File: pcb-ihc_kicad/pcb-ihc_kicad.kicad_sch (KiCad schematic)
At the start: 76 parts, among them J2 Screw_Terminal_01x01, J3 Screw_Terminal_01x01, J4 Screw_Terminal_01x01, J5 Screw_Terminal_01x01, J6 Screw_Terminal_01x01, J7 Screw_Terminal_01x01, J8 Screw_Terminal_01x01, J9 Screw_Terminal_01x01, K1 RT314A24, K2 RT314A24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

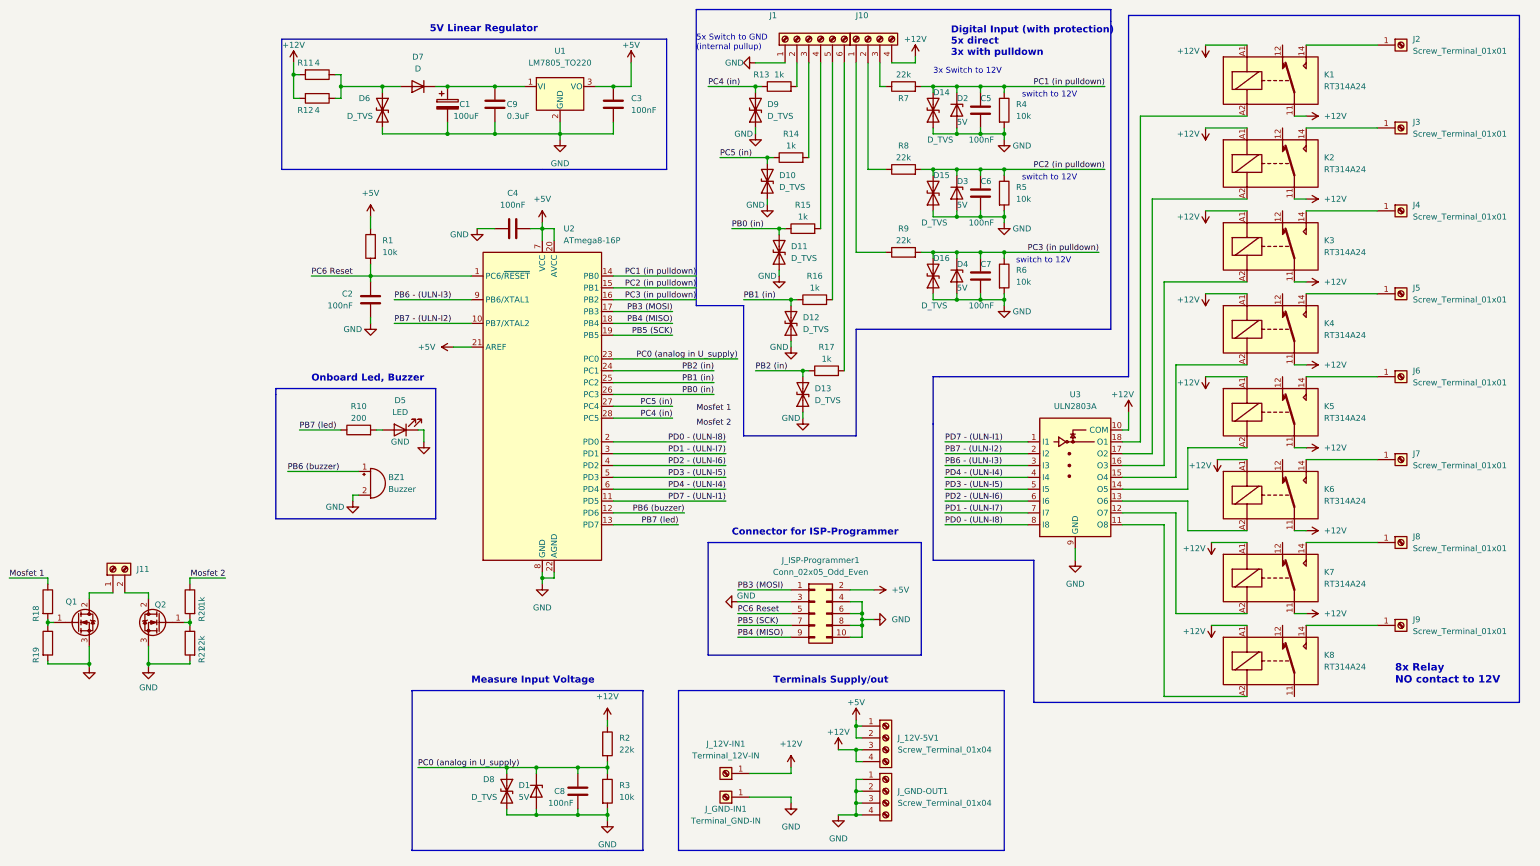
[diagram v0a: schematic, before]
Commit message: Add 2x Mosfet, Change labels, Change layout
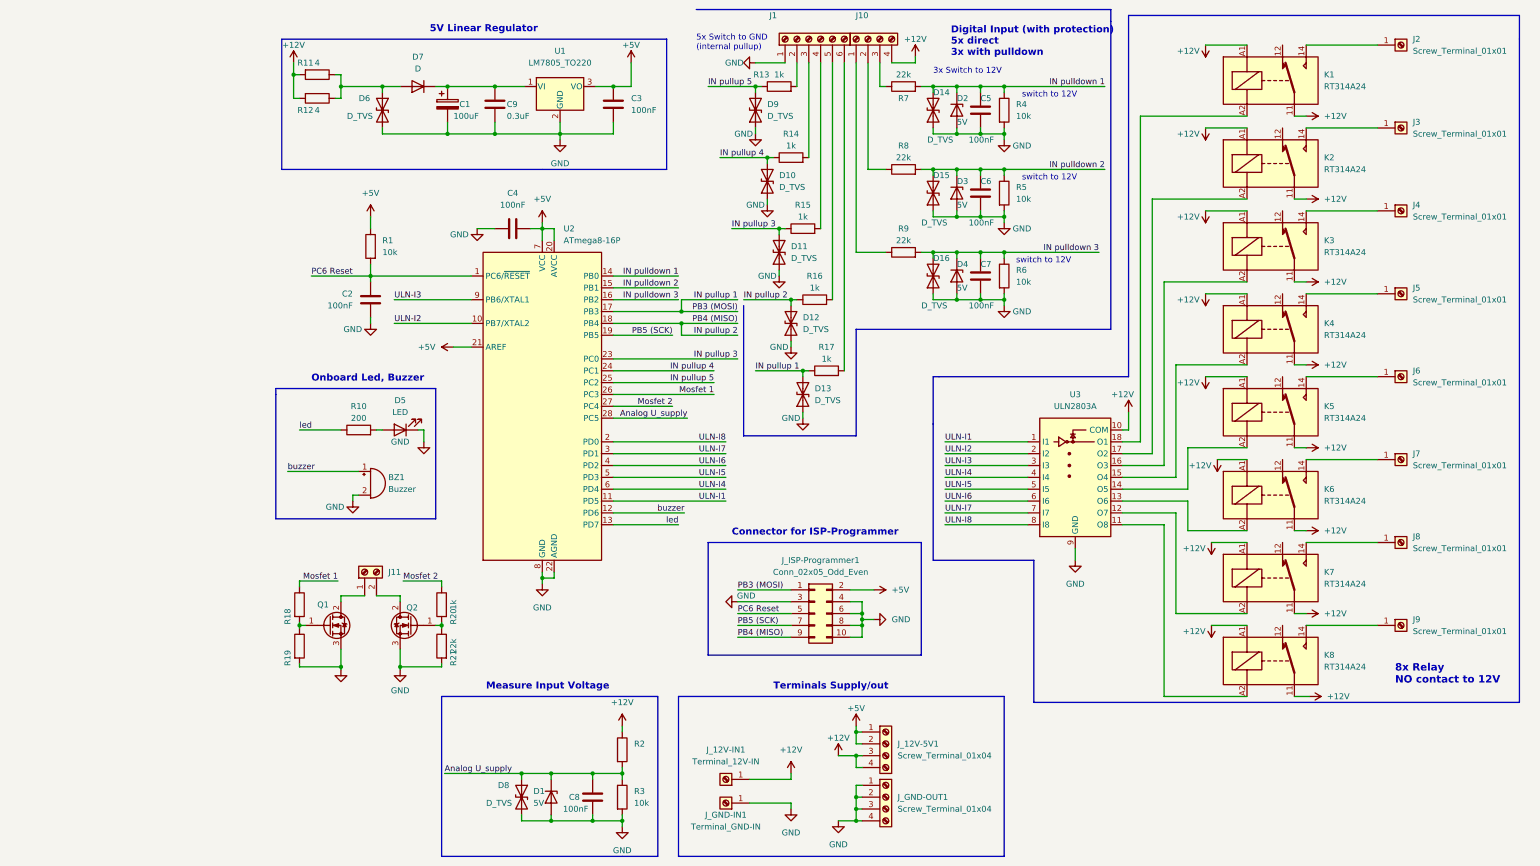
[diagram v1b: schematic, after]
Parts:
- R2: value 22k -> (none); footprint custom_footprints:my_R25-long -> (none)
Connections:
- net PB3 (MOSI) is gone; now on net IN pullup 1: J_ISP-Programmer1.1 (Pin_1), U2.17 (PB3)
- net PB4 (MISO) is gone; now on net IN pullup 2: J_ISP-Programmer1.9 (Pin_9), U2.18 (PB4)
- net +12V: now also K8.11
- net Mosfet 1: now also U2.26 (PC3)
- net Mosfet 2: now also U2.27 (PC4)
- net PB0 (in) renamed IN pullup 3
- net IN pullup 3: now also U2.23 (PC0); no longer U2.26 (PC3)
- net PB1 (in) renamed IN pullup 2
- net IN pullup 2: no longer U2.25 (PC2)
- net PB2 (in) renamed IN pullup 1
- net IN pullup 1: no longer U2.24 (PC1)
- net PB6 (buzzer) renamed buzzer
- net PB6 - (ULN-I3) renamed ULN-I3
- net PB7 (led) renamed led
- net PB7 - (ULN-I2) renamed ULN-I2
- net PC0 (analog in U_supply) renamed Analog U_supply
- net Analog U_supply: now also U2.28 (PC5); no longer U2.23 (PC0)
- net PC1 (in pulldown) renamed IN pulldown 1
- net PC2 (in pulldown) renamed IN pulldown 2
- net PC3 (in pulldown) renamed IN pulldown 3
- net PC4 (in) renamed IN pullup 5
- net IN pullup 5: now also U2.25 (PC2); no longer U2.28 (PC5)
- net PC5 (in) renamed IN pullup 4
- net IN pullup 4: now also U2.24 (PC1); no longer U2.27 (PC4)
- net PD0 - (ULN-I8) renamed ULN-I8
- net PD1 - (ULN-I7) renamed ULN-I7
- net PD2 - (ULN-I6) renamed ULN-I6
- net PD3 - (ULN-I5) renamed ULN-I5
- net PD4 - (ULN-I4) renamed ULN-I4
- net PD7 - (ULN-I1) renamed ULN-I1
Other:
- moved on the sheet: C8, D1, D8, J11, J_12V-5V1, J_12V-IN1, J_GND-IN1, J_GND-OUT1, Q1, Q2, R18, R19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

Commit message: Routing first version ready for validation
in this commit the entire routing of tracks was done. next step
validation and optimizations.
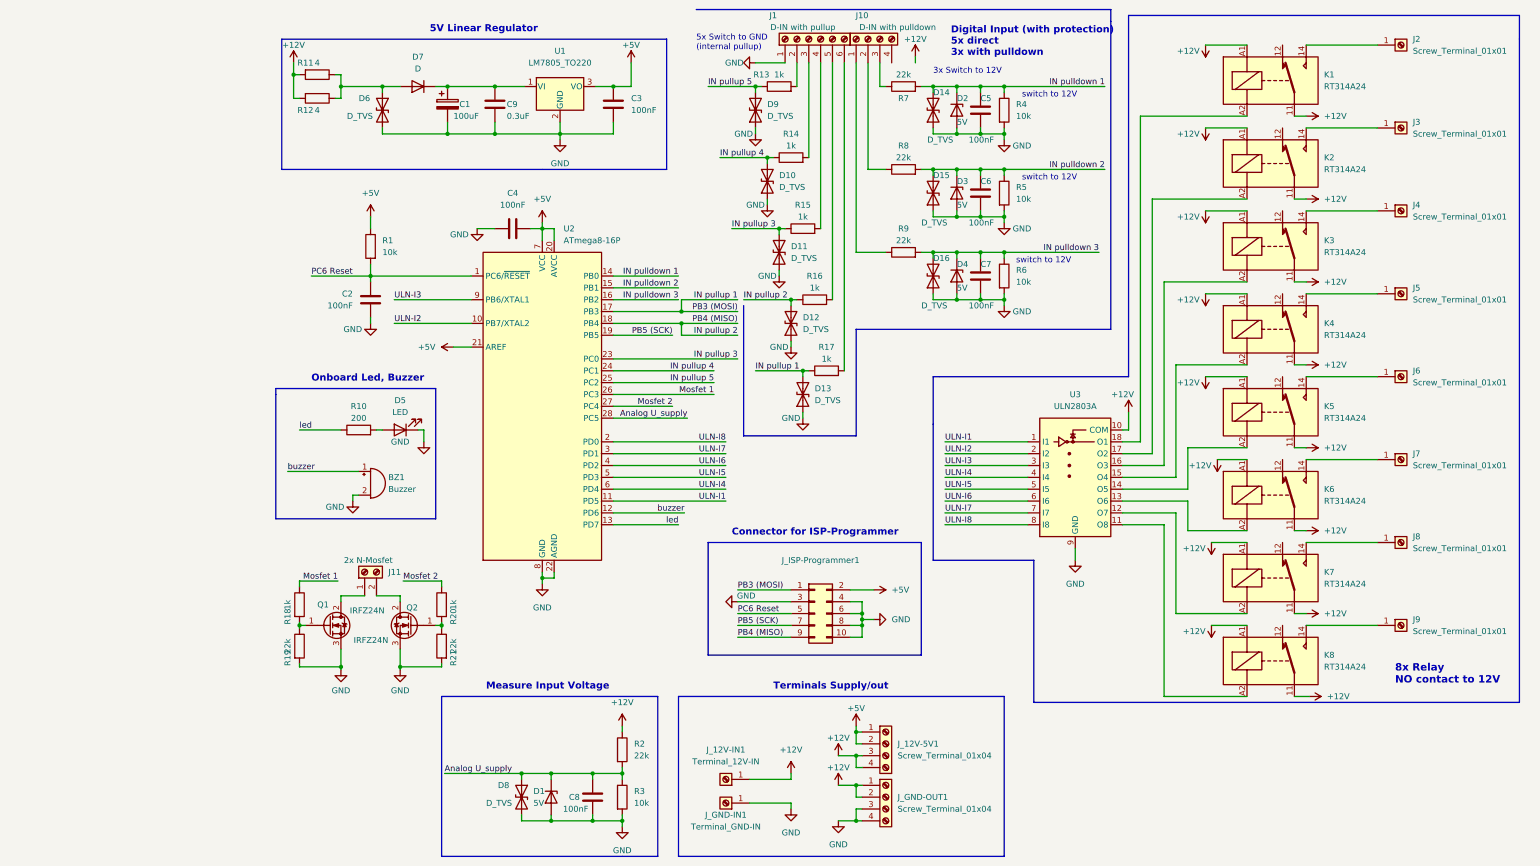
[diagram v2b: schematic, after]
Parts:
- J1: value (none) -> D-IN with pullup; footprint (none) -> TerminalBlock_WAGO:TerminalBlock_WAGO_236-406_1x06_P5.00mm_45Degree
- J10: value (none) -> D-IN with pulldown; footprint (none) -> TerminalBlock_WAGO:TerminalBlock_WAGO_236-404_1x04_P5.00mm_45Degree
- J11: value (none) -> 2x N-Mosfet; footprint (none) -> TerminalBlock_WAGO:TerminalBlock_WAGO_236-402_1x02_P5.00mm_45Degree
- J_ISP-Programmer1: value Conn_02x05_Odd_Even -> (none); footprint Connector_JST:JST_PUD_B10B-PUDSS_2x05_P2.00mm_Vertical -> (none)
- Q1: value (none) -> IRFZ24N; footprint (none) -> Package_TO_SOT_THT:TO-220-3_Vertical
- Q2: value (none) -> IRFZ24N
- R18: value (none) -> 1k
- R19: value (none) -> 22k; footprint (none) -> custom_footprints:my_R10
- R2: value (none) -> 22k; footprint (none) -> custom_footprints:my_R15-long
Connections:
- net +12V: now also J_GND-OUT1.1 (Pin_1), J_GND-OUT1.2 (Pin_2); no longer J10.4 (Pin_4)
- net GND: no longer J_GND-OUT1.1 (Pin_1), J_GND-OUT1.2 (Pin_2)
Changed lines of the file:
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@@
   (junction (at 76.2 40.64) (diameter 0) (color 0 0 0 0)
   )
-  (junction (at 139.7 182.88) (diameter 0) (color 0 0 0 0)
-  )
   (junction (at 171.45 30.48) (diameter 0) (color 0 0 0 0)
   )
@@
   (junction (at 62.23 30.48) (diameter 0) (color 0 0 0 0)
   )
-  (junction (at 139.7 185.42) (diameter 0) (color 0 0 0 0)
-  )
   (junction (at 67.945 177.8) (diameter 0) (color 0 0 0 0)
   )
@@
   (junction (at 72.39 60.96) (diameter 0) (color 0 0 0 0)
   )
+  (junction (at 139.7 180.34) (diameter 0) (color 0 0 0 0)
+  )
   (junction (at 29.21 154.94) (diameter 0) (color 0 0 0 0)
   )
@@
     (stroke (width 0) (type default) (color 0 0 0 0))
   )
-  (wire (pts (xy 139.7 185.42) (xy 139.7 182.88))
-    (stroke (width 0) (type default) (color 0 0 0 0))
-  )
   (wire (pts (xy 125.73 77.47) (xy 125.73 76.2))
     (stroke (width 0) (type default) (color 0 0 0 0))
@@
     (stroke (width 0) (type default) (color 0 0 0 0))
   )
-  (wire (pts (xy 152.4 25.4) (xy 147.32 25.4))
-    (stroke (width 0) (type default) (color 0 0 0 0))
-  )
   (wire (pts (xy 166.37 40.64) (xy 171.45 40.64))
     (stroke (width 0) (type default) (color 0 0 0 0))
@@
     (stroke (width 0) (type default) (color 0 0 0 0))
   )
+  (wire (pts (xy 135.89 180.34) (xy 139.7 180.34))
+    (stroke (width 0) (type default) (color 0 0 0 0))
+  )
   (wire (pts (xy 41.91 154.94) (xy 41.91 155.575))
     (stroke (width 0) (type default) (color 0 0 0 0))
@@
       (effects (font (size 1.27 1.27)) (justify left))
     )
-    (property "Value" "" (id 1) (at 39.37 149.225 0)
+    (property "Value" "IRFZ24N" (id 1) (at 39.37 149.225 0)
       (effects (font (size 1.27 1.27)) (justify left))
     )
@@
       (effects (font (size 1.27 1.27)) (justify left))
     )
-    (property "Value" "" (id 1) (at 31.115 142.875 0)
+    (property "Value" "IRFZ24N" (id 1) (at 31.115 142.875 0)
       (effects (font (size 1.27 1.27)) (justify left))
     )
-    (property "Footprint" "" (id 2) (at 33.02 147.955 0)
+    (property "Footprint" "Package_TO_SOT_THT:TO-220-3_Vertical" (id 2) (at 33.02 147.955 0)
       (effects (font (size 1.27 1.27) italic) (justify left) hide)
     )
@@
       (effects (font (size 1.27 1.27)) (justify right))
     )
-    (property "Value" "" (id 1) (at 29.845 132.08 90)
+    (property "Value" "2x N-Mosfet" (id 1) (at 29.845 132.08 90)
       (effects (font (size 1.27 1.27)) (justify right))
     )
-    (property "Footprint" "" (id 2) (at 34.29 134.62 0)
+    (property "Footprint" "TerminalBlock_WAGO:TerminalBlock_WAGO_236-402_1x02_P5.00mm_45Degree" (id 2) (at 34.29 134.62 0)
       (effects (font (size 1.27 1.27)) hide)
     )
@@
     (in_bom yes) (on_board yes)
     (property "Reference" "R18" (id 0) (at 17.78 144.145 90))
-    (property "Value" "" (id 1) (at 17.78 141.605 90))
+    (property "Value" "1k" (id 1) (at 17.78 141.605 90))
     (property "Footprint" "custom_footprints:my_R10" (id 2) (at 18.542 141.605 90)
       (effects (font (size 1.27 1.27)) hide)
@@
     (in_bom yes) (on_board yes) (fields_autoplaced)
     (property "Reference" "J_ISP-Programmer1" (id 0) (at 132.08 132.08 0))
-    (property "Value" "Conn_02x05_Odd_Even" (id 1) (at 132.08 134.62 0))
-    (property "Footprint" "Connector_JST:JST_PUD_B10B-PUDSS_2x05_P2.00mm_Vertical" (id 2) (at 130.81 143.51 0)
+    (property "Value" "" (id 1) (at 132.08 134.62 0))
+    (property "Footprint" "" (id 2) (at 130.81 143.51 0)
       (effects (font (size 1.27 1.27)) hide)
     )
@@
       (effects (font (size 1.27 1.27)) (justify left))
     )
-    (property "Value" "" (id 1) (at 92.075 173.9899 0)
+    (property "Value" "22k" (id 1) (at 92.075 173.9899 0)
       (effects (font (size 1.27 1.27)) (justify left))
     )
-    (property "Footprint" "" (id 2) (at 87.757 172.72 90)
+    (property "Footprint" "custom_footprints:my_R15-long" (id 2) (at 87.757 172.72 90)
       (effects (font (size 1.27 1.27)) hide)
     )
@@
     (in_bom yes) (on_board yes)
     (property "Reference" "R19" (id 0) (at 17.78 153.035 90))
-    (property "Value" "" (id 1) (at 17.78 150.495 90))
-    (property "Footprint" "" (id 2) (at 18.542 150.495 90)
+    (property "Value" "22k" (id 1) (at 17.78 150.495 90))
+    (property "Footprint" "custom_footprints:my_R10" (id 2) (at 18.542 150.495 90)
       (effects (font (size 1.27 1.27)) hide)
     )
@@
     (in_bom yes) (on_board yes)
     (property "Reference" "J1" (id 0) (at 121.92 15.24 90))
-    (property "Value" "" (id 1) (at 128.27 17.78 90))
-    (property "Footprint" "" (id 2) (at 129.54 20.32 0)
+    (property "Value" "D-IN with pullup" (id 1) (at 128.27 17.78 90))
+    (property "Footprint" "TerminalBlock_WAGO:TerminalBlock_WAGO_236-406_1x06_P5.00mm_45Degree" (id 2) (at 129.54 20.32 0)
       (effects (font (size 1.27 1.27)) hide)
     )
@@
     (pin "2")
   )
+  (symbol (lib_id "power:+12V") (at 135.89 180.34 0) (unit 1)
+    (in_bom yes) (on_board yes)
+    (property "Reference" "#PWR0152" (id 0) (at 135.89 184.15 0)
+      (effects (font (size 1.27 1.27)) hide)
+    )
+    (property "Value" "+12V" (id 1) (at 135.89 176.53 0))
+    (property "Footprint" "" (id 2) (at 135.89 180.34 0)
+      (effects (font (size 1.27 1.27)) hide)
+    )
+    (property "Datasheet" "" (id 3) (at 135.89 180.34 0)
+      (effects (font (size 1.27 1.27)) hide)
+    )
+    (pin "1")
+  )
   (symbol (lib_id "Device:C") (at 83.185 182.88 0) (unit 1)
     (in_bom yes) (on_board yes)
@@
     (in_bom yes) (on_board yes)
     (property "Reference" "J10" (id 0) (at 140.97 15.24 90))
-    (property "Value" "" (id 1) (at 148.59 17.78 90))
-    (property "Footprint" "" (id 2) (at 142.24 20.32 0)
+    (property "Value" "D-IN with pulldown" (id 1) (at 148.59 17.78 90))
+    (property "Footprint" "TerminalBlock_WAGO:TerminalBlock_WAGO_236-404_1x04_P5.00mm_45Degree" (id 2) (at 142.24 20.32 0)
       (effects (font (size 1.27 1.27)) hide)
     )
@@
       (effects (font (size 1.27 1.27)) hide)
     )
-    (property "Value" "" (id 1) (at 29.21 160.02 0))
+    (property "Value" "GND" (id 1) (at 29.21 160.02 0))
     (property "Footprint" "" (id 2) (at 29.21 155.575 0)
       (effects (font (size 1.27 1.27)) hide)
@@
       (reference "#PWR0151") (unit 1) (value "+12V") (footprint "")
     )
+    (path "/e06b988d-5c93-4204-a2b1-c895c0daeafb"
+      (reference "#PWR0152") (unit 1) (value "+12V") (footprint "")
+    )
     (path "/4f7b24c2-4bfe-4f23-a154-b1059c420795"
       (reference "BZ1") (unit 1) (value "Buzzer") (footprint "Buzzer_Beeper:Buzzer_12x9.5RM7.6")
@@
     )
     (path "/b5146f6c-0b42-45ae-b77a-459791c0c5d8"
-      (reference "J_ISP-Programmer1") (unit 1) (value "Conn_02x05_Odd_Even") (footprint "Connector_JST:JST_PUD_B10B-PUDSS_2x05_P2.00mm_Vertical")
+      (reference "J_ISP-Programmer1") (unit 1) (value "Conn_02x05_Odd_Even") (footprint "custom_footprints:my_wannenstecker_2x5")
     )
     (path "/5298adb0-830b-47ef-8abe-9e94d49af0b3"
